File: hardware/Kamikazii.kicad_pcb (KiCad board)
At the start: 4 copper layers, 88 x 54 mm, 41 parts, among them M1 Screw_Terminal_01x02, M2 Screw_Terminal_01x02, U1 L7805CV, U2 BP, U2 ROB-14450

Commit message: Finalize schematic
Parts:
- removed A1, A2: Arduino_Nano_Every, Module:Arduino_Nano
- removed C1, C2, C6: 0.1uF, Capacitor_THT:C_Disc_D3.0mm_W1.6mm_P2.50mm
- removed C3: 0.33uF, Capacitor_THT:C_Disc_D3.0mm_W1.6mm_P2.50mm
- removed C4, C5: 100uF, Capacitor_THT:C_Radial_D6.3mm_H11.0mm_P2.50mm
- removed D21, D22: LED, LED_THT:LED_D5.0mm
- removed MD1, MD2: DRV8871DDAR, DRV8871DDAR:VREG_LM5017MR_NOPB
- removed R1, R2: 2K, Resistor_THT:R_Axial_DIN0207_L6.3mm_D2.5mm_P7.62mm_Horizontal
- removed R11, R12, R13, R14, R15, R21, R22: 220, Resistor_THT:R_Axial_DIN0207_L6.3mm_D2.5mm_P7.62mm_Horizontal
- removed the U2 at (118.0, 97.0)
- removed the U2 at (213.2, 95.7)
- added C01: 330n, Capacitor_SMD:C_0402_1005Metric, F.Cu at (62.0, 113.7)
- added C02: 100n, Capacitor_SMD:C_0402_1005Metric, F.Cu at (62.0, 115.6)
- added C03: 100n, Capacitor_SMD:C_0402_1005Metric, F.Cu at (62.0, 117.6)
- added C04: 47u, Capacitor_SMD:C_1210_3225Metric, F.Cu at (73.3, 66.2)
- added C05: 100n, Capacitor_SMD:C_0402_1005Metric, F.Cu at (62.0, 119.6)
- added C06: 47u, Capacitor_SMD:C_1210_3225Metric, F.Cu at (73.3, 70.4)
- added C07: 100n, Capacitor_SMD:C_0402_1005Metric, F.Cu at (62.0, 121.5)
- added C08: 100n, Capacitor_SMD:C_0402_1005Metric, F.Cu at (62.0, 123.5)
- added C09: 100n, Capacitor_SMD:C_0402_1005Metric, F.Cu at (64.8, 113.7)
- added C10: 100n, Capacitor_SMD:C_0402_1005Metric, F.Cu at (64.8, 115.6)
- added C11: 100n, Capacitor_SMD:C_0402_1005Metric, F.Cu at (64.8, 117.6)
- added C12: 100n, Capacitor_SMD:C_0402_1005Metric, F.Cu at (64.8, 119.6)
- added C13: 100n, Capacitor_SMD:C_0402_1005Metric, F.Cu at (64.8, 121.5)
- added C14: 47u, Capacitor_SMD:C_1210_3225Metric, F.Cu at (73.3, 74.7)
- added C15: 100n, Capacitor_SMD:C_0402_1005Metric, F.Cu at (64.8, 123.5)
- added C16: 100n, Capacitor_SMD:C_0402_1005Metric, F.Cu at (67.7, 113.7)
- added C17: 470u, Capacitor_THT:CP_Radial_D8.0mm_P3.50mm, F.Cu at (72.4, 117.4)
- added C18: 100n, Capacitor_SMD:C_0402_1005Metric, F.Cu at (67.7, 115.6)
- added C19: 100n, Capacitor_SMD:C_0402_1005Metric, F.Cu at (67.7, 117.6)
- added D16: LED, LED_SMD:LED_0402_1005Metric, F.Cu at (72.2, 93.7)
- added D17: LED, LED_SMD:LED_0402_1005Metric, F.Cu at (72.2, 95.7)
- added H1: M3, MountingHole:MountingHole_3.2mm_M3, F.Cu at (118.0, 82.0)
- added H2: M3, MountingHole:MountingHole_3.2mm_M3, F.Cu at (66.5, 76.0)
- added H3: M3, MountingHole:MountingHole_3.2mm_M3, F.Cu at (66.5, 83.9)
- added H4: M3, MountingHole:MountingHole_3.2mm_M3, F.Cu at (66.5, 91.9)
- added R01: 1k, Resistor_SMD:R_0402_1005Metric, F.Cu at (72.0, 77.8)
- added R02: 1k, Resistor_SMD:R_0402_1005Metric, F.Cu at (72.0, 79.8)
- added R03: 1k, Resistor_SMD:R_0402_1005Metric, F.Cu at (72.0, 81.8)
- added R04: 1k, Resistor_SMD:R_0402_1005Metric, F.Cu at (74.9, 77.8)
- added R05: 1k, Resistor_SMD:R_0402_1005Metric, F.Cu at (74.9, 79.8)
- added R06: 1k, Resistor_SMD:R_0402_1005Metric, F.Cu at (74.9, 81.8)
- added R07: 1k, Resistor_SMD:R_0402_1005Metric, F.Cu at (77.8, 77.8)
- added R08: 30K, Resistor_SMD:R_0402_1005Metric, F.Cu at (77.8, 79.8)
- added R09: 30K, Resistor_SMD:R_0402_1005Metric, F.Cu at (77.8, 81.8)
- added SW1: 210-4MS, 210-4MS:210-4MS, F.Cu at (61.7, 102.2)
- added T1: On/Off, Connector_PinHeader_2.54mm:PinHeader_1x03_P2.54mm_Vertical, F.Cu at (53.7, 101.6)
- added T2: Remote Start, Connector_PinHeader_2.54mm:PinHeader_1x03_P2.54mm_Vertical, F.Cu at (58.2, 101.6)
- added U2: DRV8871DDAR, DRV8871DDAR:VREG_LM5017MR_NOPB, F.Cu at (75.3, 109.0)
- added U3: BP, blue_pill:blue_pill, F.Cu at (143.1, 100.9)
- added U4: L7805CV, L7805CV:TO255P1040X460X1968-3, F.Cu at (45.6, 121.4)
- D11, D12, D13, D14, D15: footprint LED_THT:LED_D5.0mm -> LED_SMD:LED_0402_1005Metric
- JB1: value Conn_01x02 -> XT30
- M1, M2: value Screw_Terminal_01x02 -> Motor
- S1, S2: value Screw_Terminal_01x02 -> Servo; footprint TerminalBlock:TerminalBlock_Xinya_XY308-2.54-2P_1x02_P2.54mm_Horizontal -> Connector_PinHeader_2.54mm:PinHeader_1x03_P2.54mm_Vertical
- U1: value L7805CV -> DRV8871DDAR; footprint L7805CV:TO255P1040X460X1968-3 -> DRV8871DDAR:VREG_LM5017MR_NOPB
- moved S2 206.3 mm to (49.1, 101.6)
- moved S1 203.3 mm to (44.5, 101.6)
- moved JB1 161.0 mm to (28.1, 118.5), turned to 0 degrees
- moved L1 134.1 mm to (54.9, 77.0), turned to 0 degrees
- moved M2 123.2 mm to (52.4, 113.1)
- moved D5 116.4 mm to (54.9, 68.2)
- moved D4 115.4 mm to (44.7, 94.6)
- moved U1 105.0 mm to (75.3, 102.5), turned to 0 degrees
- moved D3 102.5 mm to (44.7, 85.8)
- moved D15 98.1 mm to (72.2, 91.7)
- moved D2 90.2 mm to (44.7, 77.0)
- moved D14 90.2 mm to (72.2, 89.8)
- moved D13 82.4 mm to (72.2, 87.8)
- moved D1 79.8 mm to (44.7, 68.2)
- moved M1 76.0 mm to (44.7, 113.1)
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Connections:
- D1 pad 2: unconnected-(D1-Pin_2-Pad2) -> /D101
- D2 pad 2: unconnected-(D2-Pin_2-Pad2) -> /D102
- D3 pad 2: unconnected-(D3-Pin_2-Pad2) -> /D103
- D4 pad 2: unconnected-(D4-Pin_2-Pad2) -> /D104
- D5 pad 2: unconnected-(D5-Pin_2-Pad2) -> /D105
- JB1 pad 1: Net-(JB1-Pin_1) -> VBAT
- L1 pad 3: unconnected-(L1-Pin_3-Pad3) -> /L101
- L2 pad 3: unconnected-(L2-Pin_3-Pad3) -> /L102
- S1 pad 1: Net-(MD2-OUT1) -> /S101
- S1 pad 2: Net-(MD2-OUT2) -> 5V
- S2 pad 1: Net-(MD1-OUT1) -> /S102
- S2 pad 2: Net-(MD1-OUT2) -> 5V
- U1 pad 1: Net-(U1-INPUT) -> GND
- U1 pad 2: GND -> /M102
- U1 pad 3: 5V -> /M101
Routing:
- net 5V: track 209.4 -> 0.00 mm
- net Net-(JB1-Pin_1): track 111.1 -> 0.00 mm
- net Net-(M2-Pin_2): track 102.5 -> 0.00 mm
- net Net-(M2-Pin_1): track 93.1 -> 0.00 mm
- net /D8: track 40.6 -> 0.00 mm
- net Net-(M1-Pin_2): track 35.6 -> 0.00 mm
- net /A0: track 32.6 -> 0.00 mm
- net Net-(A2-D7): track 32.3 -> 0.00 mm
- net /D2: track 31.5 -> 0.00 mm
- net /D10: track 30.1 -> 0.00 mm
- net Net-(M1-Pin_1): track 30.0 -> 0.00 mm
- net /A7: track 26.0 -> 0.00 mm
- net Net-(A2-D6): track 24.6 -> 0.00 mm
- net Net-(A2-D3): track 24.6 -> 0.00 mm
- net /D9: track 22.9 -> 0.00 mm
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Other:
- board size 88 x 54 mm -> 75 x 49 mm
- board text removed: "Jaeyoung Choi"

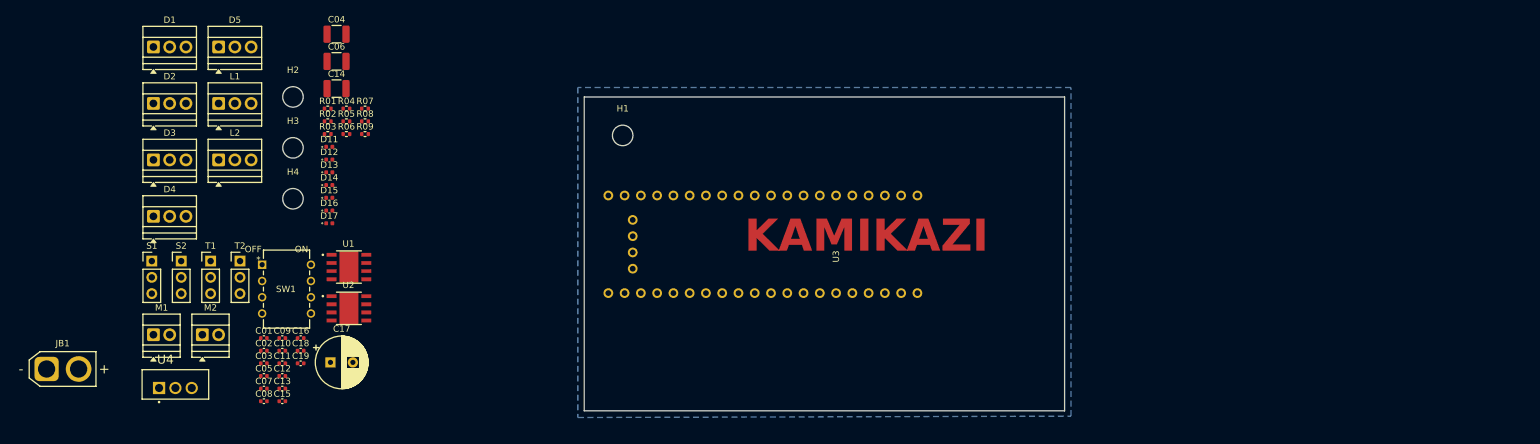
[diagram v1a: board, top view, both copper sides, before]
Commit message: Start routing and fix minor schematic mistakes
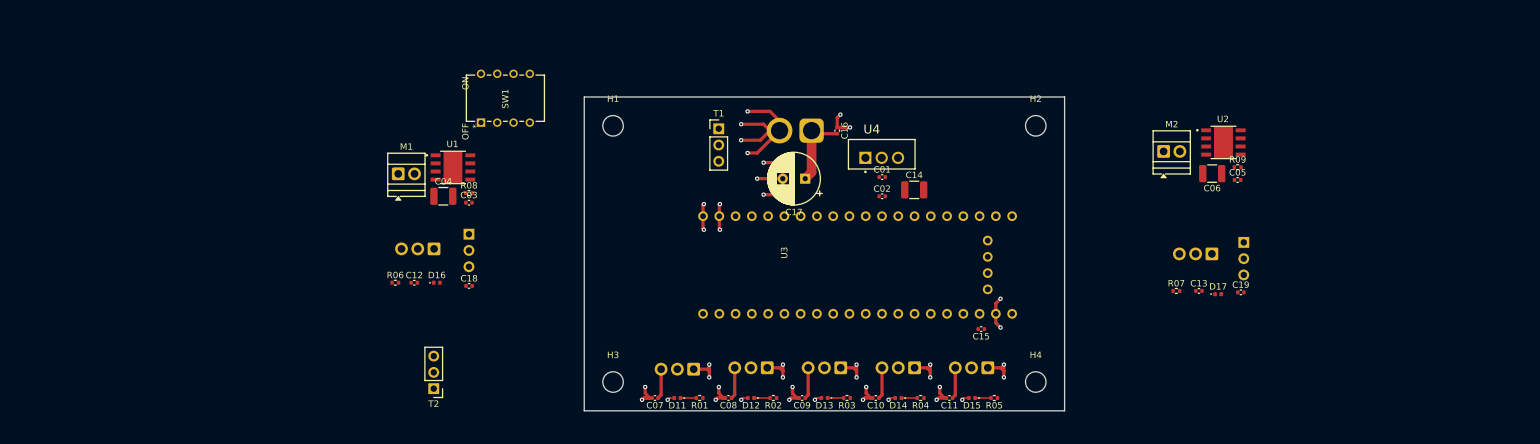
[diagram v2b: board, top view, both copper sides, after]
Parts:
- D1, D2, D3, D4, D5, JB1, L1, L2, S1, S2: moved to B.Cu
- moved S2 165.9 mm to (215.0, 98.7), turned to 180 degrees
- moved L2 155.8 mm to (210.0, 100.5), turned to 180 degrees
- moved C05 155.1 mm to (214.0, 89.0)
- moved M2 152.8 mm to (202.5, 84.5)
- moved C19 147.2 mm to (214.5, 106.5)
- moved C13 143.9 mm to (208.0, 106.3)
- moved D17 139.2 mm to (211.0, 106.8)
- moved U2 139.0 mm to (211.8, 83.1)
- moved C06 137.8 mm to (210.1, 88.0), turned to 180 degrees
- moved R09 136.4 mm to (214.0, 87.0)
- moved D5 130.1 mm to (175.0, 118.3), turned to 180 degrees
- moved R07 129.8 mm to (204.4, 106.3)
- moved JB1 125.1 mm to (147.5, 81.2), turned to 180 degrees
- moved D4 121.2 mm to (163.6, 118.3), turned to 180 degrees
- moved H4 119.5 mm to (182.5, 120.5)
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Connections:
- T1 pad 2: Net-(T1-Pin_2) -> VBAT
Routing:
- net GND: track 0.00 -> 108.1 mm, vias 0 -> 40
- net 5V: track 0.00 -> 24.4 mm
- net VBAT: track 0.00 -> 12.1 mm
- net Net-(D13-K): track 0.00 -> 2.52 mm
- net Net-(D11-K): track 0.00 -> 2.49 mm
- net Net-(D15-K): track 0.00 -> 2.49 mm
- net Net-(D14-K): track 0.00 -> 2.49 mm
- net Net-(D12-K): track 0.00 -> 2.49 mm
- added copper zone on In1.Cu, net GND
- removed copper zone on B.Cu, net GND
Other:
- rule solder_mask_min_width: 0.12 -> 0.1016
- board text removed: "KAMIKAZI"

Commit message: Make minor adjustments to schematic and finish layout with no errors
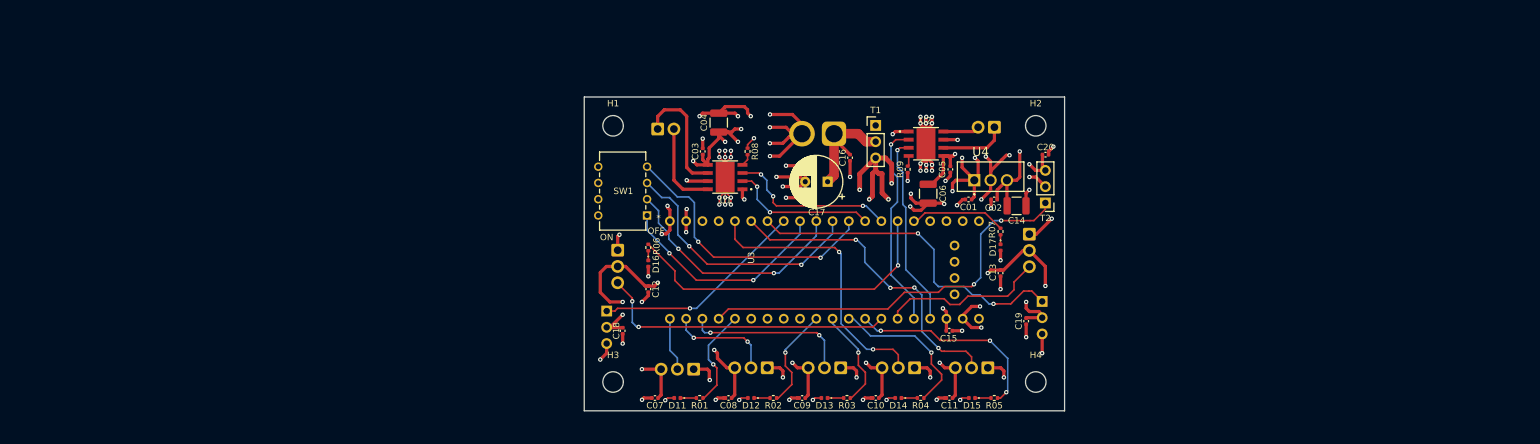
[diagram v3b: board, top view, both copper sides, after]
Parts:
- added C20: 100n, Capacitor_SMD:C_0402_1005Metric, F.Cu at (184.0, 85.0)
- M1, M2: moved to B.Cu
- moved T2 99.8 mm to (184.0, 92.5)
- moved R09 51.5 mm to (162.5, 87.3), turned to 90 degrees
- moved U2 46.4 mm to (165.4, 83.3)
- moved C05 44.9 mm to (169.2, 87.3), turned to -90 degrees
- moved C04 44.5 mm to (133.0, 80.0), turned to 90 degrees
- moved C06 44.5 mm to (165.7, 91.1), turned to -90 degrees
- moved R08 44.0 mm to (137.5, 84.5), turned to -90 degrees
- moved U1 42.5 mm to (134.0, 88.5), turned to 180 degrees
- moved M1 41.1 mm to (123.5, 81.0)
- moved R06 39.9 mm to (122.0, 99.5), turned to -90 degrees
- moved C03 37.4 mm to (130.5, 84.5), turned to 90 degrees
- moved C12 36.5 mm to (122.0, 106.0), turned to -90 degrees
- moved D17 34.7 mm to (177.0, 99.5), turned to -90 degrees
- moved C19 33.8 mm to (181.0, 111.0), turned to 90 degrees
- moved D16 33.2 mm to (122.0, 102.0), turned to -90 degrees
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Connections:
- U3 pad PA0: /LED106 -> /LED107
- U3 pad PA1: /LED107 -> /LED106
- U3 pad PB10: /D101 -> /D105
- U3 pad PB11: /D102 -> /D104
- U3 pad PB12: /D103 -> /D101
- U3 pad PB13: /D104 -> /D102
- U3 pad PB14: /D105 -> /D103
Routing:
- net GND: track 108.1 -> 234.6 mm, vias 40 -> 87
- net 5V: track 24.4 -> 109.1 mm, vias 0 -> 14
- net 9V: track 0.00 -> 70.4 mm, vias 0 -> 12
- net /R101: track 0.00 -> 63.0 mm, vias 0 -> 2
- net /S102: track 0.00 -> 52.7 mm, vias 0 -> 2
- net /LED106: track 0.00 -> 51.3 mm, vias 0 -> 1
- net /D105: track 0.00 -> 49.8 mm, vias 0 -> 4
- net /L101: track 0.00 -> 46.9 mm, vias 0 -> 2
- net /D104: track 0.00 -> 44.2 mm, vias 0 -> 2
- net /SW104: track 0.00 -> 43.7 mm, vias 0 -> 2
- net /SW103: track 0.00 -> 40.9 mm, vias 0 -> 2
- net /SW102: track 0.00 -> 37.6 mm, vias 0 -> 2
- net /SW101: track 0.00 -> 34.5 mm, vias 0 -> 2
- net /S101: track 0.00 -> 34.1 mm, vias 0 -> 1
- net /M104: track 0.00 -> 32.6 mm, vias 0 -> 1
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- added copper zone on In2.Cu, net 5V
- added copper zone on In2.Cu, net 9V
- added copper zone on In2.Cu, net GND
